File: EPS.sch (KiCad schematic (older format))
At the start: 35 parts, among them J1 Conn_01x07_Male, J2 Conn_01x03_Male, J3 Conn_01x03_Male, J4 Screw_Terminal_01x02, J5 Screw_Terminal_01x02, U1 AD5245, U2 LM2936-3.3, U3 LT8611

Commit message: Modified schematic to pass electrical rules check
Added power flags. Resolved error due to stacked power output pins
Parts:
- removed U3: LT8611, HS2_parts:24-QFN_3x5, symbol MPPTCharger:LT8611
- added U3: LT8611, HS2_parts:24-QFN_3x5, symbol HS2_Parts:LT8611
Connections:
- wire segments 49 -> 53
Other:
- moved on the sheet: C3, D5, R6
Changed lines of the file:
@@
 L Device:C_Small C3
 U 1 1 5FC2211C
-P 6400 4200
-F 0 "C3" V 6171 4200 50  0000 C CNN
-F 1 "1u" V 6262 4200 50  0000 C CNN
-F 2 "Capacitor_SMD:C_0805_2012Metric_Pad1.15x1.40mm_HandSolder" H 6400 4200 50  0001 C CNN
-F 3 "~" H 6400 4200 50  0001 C CNN
-	1    6400 4200
-	0    1    1    0
+P 6150 4100
+F 0 "C3" V 5921 4100 50  0000 C CNN
+F 1 "1u" V 6012 4100 50  0000 C CNN
+F 2 "Capacitor_SMD:C_0805_2012Metric_Pad1.15x1.40mm_HandSolder" H 6150 4100 50  0001 C CNN
+F 3 "~" H 6150 4100 50  0001 C CNN
+	1    6150 4100
+	-1   0    0    1
 $EndComp
 $Comp
 L power:GND #PWR014
 U 1 1 5FC22EAF
-P 6300 4200
-F 0 "#PWR014" H 6300 3950 50  0001 C CNN
-F 1 "GND" V 6305 4072 50  0000 R CNN
-F 2 "" H 6300 4200 50  0001 C CNN
-F 3 "" H 6300 4200 50  0001 C CNN
-	1    6300 4200
-	0    1    1    0
-$EndComp
-$Comp
-L MPPTCharger:LT8611 U3
-U 1 1 5FC1D006
-P 7000 4000
-F 0 "U3" H 6937 4625 50  0000 C CNN
-F 1 "LT8611" H 6937 4534 50  0000 C CNN
-F 2 "HS2_parts:24-QFN_3x5" H 7200 4500 50  0001 C CNN
-F 3 "" H 7200 4500 50  0001 C CNN
-	1    7000 4000
-	1    0    0    -1
+P 6150 4000
+F 0 "#PWR014" H 6150 3750 50  0001 C CNN
+F 1 "GND" V 6155 3872 50  0000 R CNN
+F 2 "" H 6150 4000 50  0001 C CNN
+F 3 "" H 6150 4000 50  0001 C CNN
+	1    6150 4000
+	-1   0    0    1
 $EndComp
 $Comp
@@
 U 1 1 5FC2394E
 P 6400 4400
-F 0 "R5" V 6204 4400 50  0000 C CNN
-F 1 "60.4k" V 6295 4400 50  0000 C CNN
+F 0 "R5" V 6350 4350 50  0000 C CNN
+F 1 "60.4k" V 6500 4350 50  0000 C CNN
 F 2 "Resistor_SMD:R_0805_2012Metric_Pad1.15x1.40mm_HandSolder" H 6400 4400 50  0001 C CNN
 F 3 "~" H 6400 4400 50  0001 C CNN
@@
 Text Label 4850 4600 2    50   ~ 0
 SCL
-Text Label 4850 4400 2    50   ~ 0
+Text Label 4750 4400 2    50   ~ 0
 VDD
 Text Label 5450 4600 0    50   ~ 0
@@
 $EndComp
 NoConn ~ 6500 4100
-Text Label 6500 4500 2    50   ~ 0
+Text Label 6500 4650 2    50   ~ 0
 PG
 $Comp
 L Device:R_Small R6
 U 1 1 5FC4E4AA
-P 6500 4600
-F 0 "R6" H 6441 4554 50  0000 R CNN
-F 1 "10k" H 6441 4645 50  0000 R CNN
-F 2 "Resistor_SMD:R_0805_2012Metric_Pad1.15x1.40mm_HandSolder" H 6500 4600 50  0001 C CNN
-F 3 "~" H 6500 4600 50  0001 C CNN
-	1    6500 4600
+P 6500 4900
+F 0 "R6" H 6441 4854 50  0000 R CNN
+F 1 "10k" H 6441 4945 50  0000 R CNN
+F 2 "Resistor_SMD:R_0805_2012Metric_Pad1.15x1.40mm_HandSolder" H 6500 4900 50  0001 C CNN
+F 3 "~" H 6500 4900 50  0001 C CNN
+	1    6500 4900
 	-1   0    0    1
 $EndComp
@@
 L Device:LED D5
 U 1 1 5FC4EB3B
-P 6500 4850
-F 0 "D5" V 6447 4930 50  0000 L CNN
-F 1 "LED" V 6538 4930 50  0000 L CNN
-F 2 "LED_SMD:LED_0805_2012Metric_Pad1.15x1.40mm_HandSolder" H 6500 4850 50  0001 C CNN
-F 3 "~" H 6500 4850 50  0001 C CNN
-	1    6500 4850
+P 6500 5150
+F 0 "D5" V 6447 5230 50  0000 L CNN
+F 1 "LED" V 6538 5230 50  0000 L CNN
+F 2 "LED_SMD:LED_0805_2012Metric_Pad1.15x1.40mm_HandSolder" H 6500 5150 50  0001 C CNN
+F 3 "~" H 6500 5150 50  0001 C CNN
+	1    6500 5150
 	0    1    1    0
 $EndComp
@@
 L power:+VDC #PWR017
 U 1 1 5FC4FA50
-P 6500 5000
-F 0 "#PWR017" H 6500 4900 50  0001 C CNN
-F 1 "+VDC" H 6500 5275 50  0000 C CNN
-F 2 "" H 6500 5000 50  0001 C CNN
-F 3 "" H 6500 5000 50  0001 C CNN
-	1    6500 5000
+P 6500 5300
+F 0 "#PWR017" H 6500 5200 50  0001 C CNN
+F 1 "+VDC" H 6500 5575 50  0000 C CNN
+F 2 "" H 6500 5300 50  0001 C CNN
+F 3 "" H 6500 5300 50  0001 C CNN
+	1    6500 5300
 	-1   0    0    1
 $EndComp
@@
 	1    0    0    -1
 $EndComp
-$Comp
-L power:+VDC #PWR03
-U 1 1 5FC5825F
-P 4850 3200
-F 0 "#PWR03" H 4850 3100 50  0001 C CNN
-F 1 "+VDC" V 4850 3429 50  0000 L CNN
-F 2 "" H 4850 3200 50  0001 C CNN
-F 3 "" H 4850 3200 50  0001 C CNN
-	1    4850 3200
-	0    -1   -1   0
-$EndComp
 Connection ~ 4850 3200
 $Comp
@@
 	1    0    0    -1
 $EndComp
-Wire Wire Line
-	4500 4400 4850 4400
 $Comp
 L power:+3.3V #PWR02
@@
 Text Label 8450 3000 0    50   ~ 0
 VPAN
+$Comp
+L power:PWR_FLAG #FLG0101
+U 1 1 5FC7B7BD
+P 4750 2650
+F 0 "#FLG0101" H 4750 2725 50  0001 C CNN
+F 1 "PWR_FLAG" H 4750 2823 50  0000 C CNN
+F 2 "" H 4750 2650 50  0001 C CNN
+F 3 "~" H 4750 2650 50  0001 C CNN
+	1    4750 2650
+	1    0    0    -1
+$EndComp
+$Comp
+L power:+VDC #PWR03
+U 1 1 5FC5825F
+P 4850 3200
+F 0 "#PWR03" H 4850 3100 50  0001 C CNN
+F 1 "+VDC" V 4850 3429 50  0000 L CNN
+F 2 "" H 4850 3200 50  0001 C CNN
+F 3 "" H 4850 3200 50  0001 C CNN
+	1    4850 3200
+	0    -1   -1   0
+$EndComp
+$Comp
+L power:+VDC #PWR0101
+U 1 1 5FC80A2E
+P 4400 2650
+F 0 "#PWR0101" H 4400 2550 50  0001 C CNN
+F 1 "+VDC" H 4400 2925 50  0000 C CNN
+F 2 "" H 4400 2650 50  0001 C CNN
+F 3 "" H 4400 2650 50  0001 C CNN
+	1    4400 2650
+	1    0    0    -1
+$EndComp
+$Comp
+L power:GND #PWR0102
+U 1 1 5FC810DD
+P 4750 2700
+F 0 "#PWR0102" H 4750 2450 50  0001 C CNN
+F 1 "GND" H 4755 2527 50  0000 C CNN
+F 2 "" H 4750 2700 50  0001 C CNN
+F 3 "" H 4750 2700 50  0001 C CNN
+	1    4750 2700
+	1    0    0    -1
+$EndComp
+Wire Wire Line
+	4750 2650 4750 2700
+$Comp
+L power:PWR_FLAG #FLG0102
+U 1 1 5FC8228F
+P 4400 2700
+F 0 "#FLG0102" H 4400 2775 50  0001 C CNN
+F 1 "PWR_FLAG" H 4400 2873 50  0000 C CNN
+F 2 "" H 4400 2700 50  0001 C CNN
+F 3 "~" H 4400 2700 50  0001 C CNN
+	1    4400 2700
+	-1   0    0    1
+$EndComp
+Wire Wire Line
+	4400 2650 4400 2700
+Wire Wire Line
+	4850 4400 4500 4400
+Text Label 6450 4200 2    50   ~ 0
+INTVCC
+Wire Wire Line
+	6500 4500 6500 4800
+Wire Wire Line
+	6150 4200 6500 4200
+$Comp
+L power:PWR_FLAG #FLG0103
+U 1 1 5FC8C82C
+P 4200 2700
+F 0 "#FLG0103" H 4200 2775 50  0001 C CNN
+F 1 "PWR_FLAG" H 4200 2873 50  0000 C CNN
+F 2 "" H 4200 2700 50  0001 C CNN
+F 3 "~" H 4200 2700 50  0001 C CNN
+	1    4200 2700
+	-1   0    0    1
+$EndComp
+Text Label 4200 2700 0    50   ~ 0
+VDD
+$Comp
+L HS2_Parts:LT8611 U3
+U 1 1 5FC9340A
+P 7000 4000
+F 0 "U3" H 6937 4625 50  0000 C CNN
+F 1 "LT8611" H 6937 4534 50  0000 C CNN
+F 2 "HS2_parts:24-QFN_3x5" H 7200 4500 50  0001 C CNN
+F 3 "" H 7200 4500 50  0001 C CNN
+	1    7000 4000
+	1    0    0    -1
+$EndComp
 $EndSCHEMATC

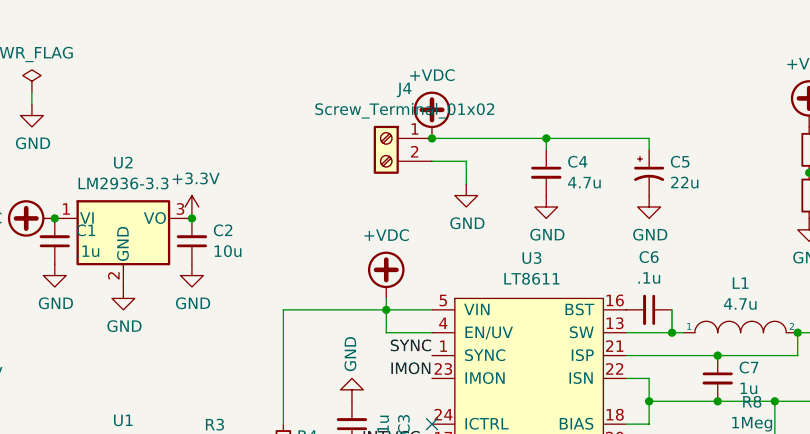
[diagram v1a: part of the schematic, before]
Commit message: Tweaked polygons and silkscreen
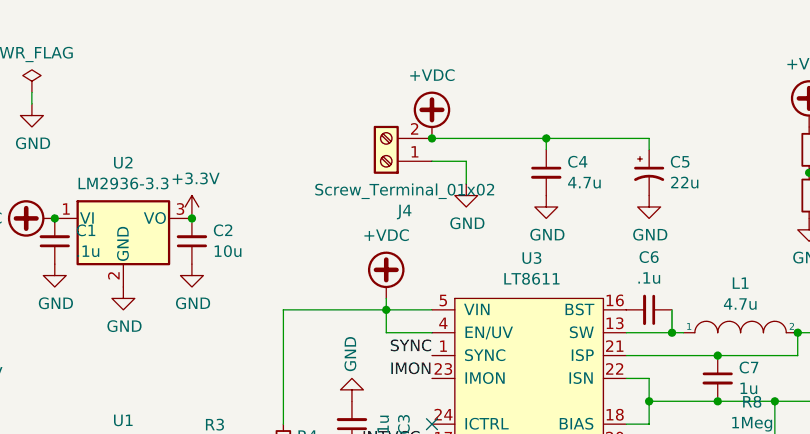
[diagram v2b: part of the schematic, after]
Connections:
- net +VDC: now also J4.2 (Pin_2); no longer J4.1 (Pin_1)
- net GND: now also J4.1 (Pin_1); no longer J4.2 (Pin_2)
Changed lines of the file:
@@
 L Connector:Screw_Terminal_01x02 J4
 U 1 1 5FC19214
-P 6300 2850
-F 0 "J4" H 6218 3067 50  0000 C CNN
-F 1 "Screw_Terminal_01x02" H 6218 2976 50  0000 C CNN
-F 2 "TerminalBlock_Phoenix:TerminalBlock_Phoenix_PT-1,5-2-3.5-H_1x02_P3.50mm_Horizontal" H 6300 2850 50  0001 C CNN
-F 3 "~" H 6300 2850 50  0001 C CNN
-	1    6300 2850
-	-1   0    0    -1
+P 6300 2950
+F 0 "J4" H 6218 3167 50  0000 C CNN
+F 1 "Screw_Terminal_01x02" H 6218 3076 50  0000 C CNN
+F 2 "TerminalBlock_Phoenix:TerminalBlock_Phoenix_PT-1,5-2-3.5-H_1x02_P3.50mm_Horizontal" H 6300 2950 50  0001 C CNN
+F 3 "~" H 6300 2950 50  0001 C CNN
+	1    6300 2950
+	-1   0    0    1
 $EndComp
 $Comp
